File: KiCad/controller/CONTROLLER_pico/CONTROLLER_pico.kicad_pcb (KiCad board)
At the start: 4 copper layers, 22 x 64 mm, 7 parts, among them J1 XF2J-1824-12A, J3 jack2.5_PJ-210B, J4 Conn_01x20_Male, J5 Conn_01x20_Male, J6 Conn_01x03_Male, J7 Conn_01x03_Male

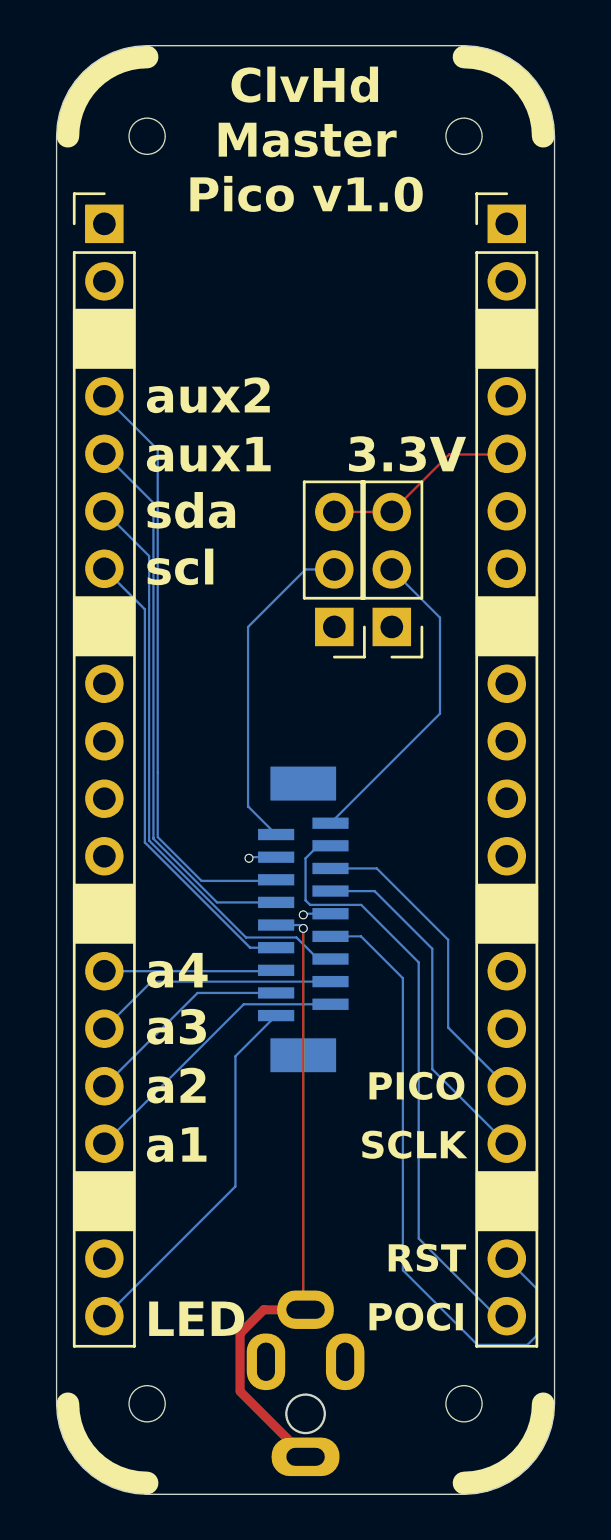
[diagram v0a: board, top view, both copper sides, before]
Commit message: fixed pico controller shield to match v3 modules
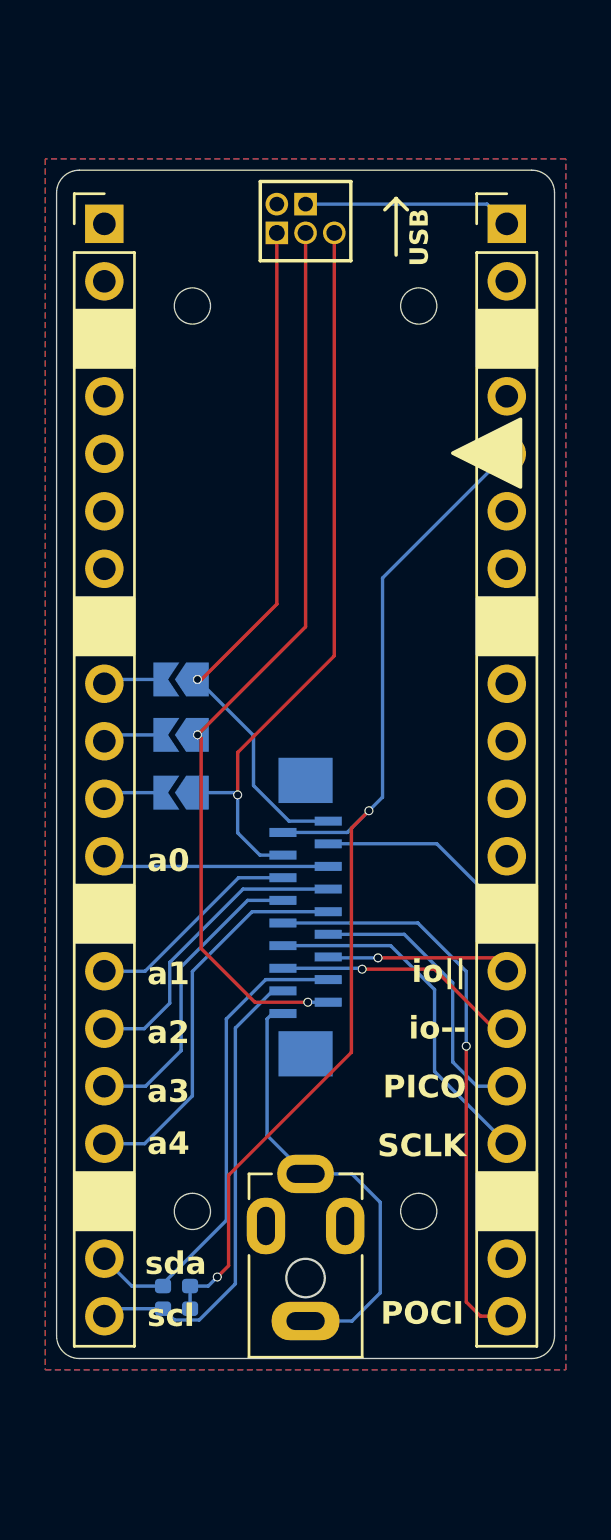
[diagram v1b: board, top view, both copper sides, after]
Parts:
- removed J6, J7: Conn_01x03_Male, Connector_PinHeader_2.54mm:PinHeader_1x03_P2.54mm_Vertical
- added FPC1: FPC-05F-18PH20, 00_lcsc:FPC-SMD_18P-P0.50_X05C2018TZ, B.Cu at (100.0, 92.5)
- added J2: jack2.5_PJ-210B, 00_custom-footprints:Jack_Socket_PJ-210B, F.Cu at (100.0, 111.9)
- added JP2: SolderJumper_2_Open, Jumper:SolderJumper-2_P1.3mm_Open_TrianglePad1.0x1.5mm, B.Cu at (94.5, 82.0)
- added JP3: SolderJumper_2_Open, Jumper:SolderJumper-2_P1.3mm_Open_TrianglePad1.0x1.5mm, B.Cu at (94.5, 84.5)
- added JP4: SolderJumper_2_Open, Jumper:SolderJumper-2_P1.3mm_Open_TrianglePad1.0x1.5mm, B.Cu at (94.5, 87.0)
- added R1: 2k, Resistor_SMD:R_0402_1005Metric_Pad0.72x0.64mm_HandSolder, B.Cu at (94.3, 109.8)
- added R2: 2k, Resistor_SMD:R_0402_1005Metric_Pad0.72x0.64mm_HandSolder, B.Cu at (94.3, 108.8)
- J1: value XF2J-1824-12A -> Conn_01x02_Pin; footprint 00_custom-footprints:XF2J-1824-12A -> Connector_PinHeader_1.27mm:PinHeader_1x02_P1.27mm_Vertical; moved to F.Cu
- J3: value jack2.5_PJ-210B -> Conn_01x03_Pin; footprint 00_custom-footprints:Jack_Socket_PJ-210B -> Connector_PinSocket_1.27mm:PinSocket_1x03_P1.27mm_Vertical; moved to F.Cu
- moved J3 55.7 mm to (98.7, 62.3), turned to 90 degrees
- moved J1 31.6 mm to (100.0, 61.0)
- moved G*** 14.0 mm to (100.0, 76.0)
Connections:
- J1 pad 1: +3.3V -> VSYS
- J1 pad 2: +5VA -> GND
- J3 pad 1: GND -> /AUX1
- J3 pad 2: IN_ref -> /AUX2
- J3 pad 3: GND -> /AUX3
- J4 pad 10: unconnected-(J4-Pin_10-Pad10) -> Net-(J4-Pin_10)
- J4 pad 11: unconnected-(J4-Pin_11-Pad11) -> Net-(J4-Pin_11)
- J4 pad 12: unconnected-(J4-Pin_12-Pad12) -> /addr_bus_0
- J4 pad 14: ADD_OUT4 -> /addr_bus_1
- J4 pad 15: ADD_OUT3 -> /addr_bus_2
- J4 pad 16: ADD_OUT2 -> /addr_bus_3
- J4 pad 17: ADD_OUT1 -> /addr_bus_4
- J4 pad 19: unconnected-(J4-Pin_19-Pad19) -> /I2C_SDA
- J4 pad 20: LED_OUT -> /i2C_SCL
- J4 pad 4: AUX2 -> unconnected-(J4-Pin_4-Pad4)
- J4 pad 5: AUX1 -> unconnected-(J4-Pin_5-Pad5)
- J4 pad 6: I2C_SDA -> unconnected-(J4-Pin_6-Pad6)
- J4 pad 7: I2C_SCL -> unconnected-(J4-Pin_7-Pad7)
- J4 pad 9: unconnected-(J4-Pin_9-Pad9) -> Net-(J4-Pin_9)
- J5 pad 1: unconnected-(J5-Pin_1-Pad1) -> VSYS
- J5 pad 14: unconnected-(J5-Pin_14-Pad14) -> /IO1_out
- J5 pad 15: unconnected-(J5-Pin_15-Pad15) -> /IO2
- J5 pad 16: PICO_DIN -> /PICO
- J5 pad 17: SCLK -> /SCLK
- J5 pad 19: RESETB -> unconnected-(J5-Pin_19-Pad19)
- J5 pad 20: POCI_DOUT -> /POCI
- J5 pad 5: 3V3_PICO -> +3.3V
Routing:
- net /AUX2: track 0.00 -> 40.3 mm, vias 0 -> 2
- net +3.3V: track 14.8 -> 48.2 mm, vias 0 -> 2
- net /AUX3: track 0.00 -> 32.5 mm, vias 0 -> 1
- net /AUX1: track 0.00 -> 30.9 mm, vias 0 -> 1
- net RESETB: track 28.3 -> 0.00 mm
- net IN_ref: track 28.1 -> 0.00 mm, vias 1 -> 0
- net POCI_DOUT: track 26.8 -> 0.00 mm
- net AUX2: track 26.5 -> 0.00 mm
- net /POCI: track 0.00 -> 25.6 mm, vias 0 -> 1
- net I2C_SDA: track 25.5 -> 0.00 mm
- net AUX1: track 24.5 -> 0.00 mm
- net /I2C_SDA: track 0.00 -> 21.3 mm
- net /i2C_SCL: track 0.00 -> 20.9 mm
- net I2C_SCL: track 20.6 -> 0.00 mm
- net /extRef: track 0.00 -> 20.0 mm
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- added copper zone on B.Cu, net GND
- added copper zone on F.Cu, net GND
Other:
- board size 22 x 64 mm -> 22 x 52.5 mm
- board text added: "ClvHd Master Pico v2.0"
- board text added: "USB"
- board text added: "a0"
- board text added: "aux"
- board text added: "io--"
- board text added: "io||"
- board text removed: "3.3V"
- board text removed: "A"
- board text removed: "ClvHd Master Pico v1.0"
- board text removed: "LED"
- board text removed: "RST"
- board text removed: "aux1"
- board text removed: "aux2"
- board text removed: "io"
